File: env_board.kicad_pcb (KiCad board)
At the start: 2 copper layers, 20.7 x 19.2 mm, 22 parts, among them J1 CONN_01X07, J2 BATT_CONN, P1 USB_OTG, Q1 Q_NMOS_GSD, Q2 Q_PMOS_GSD, U1 RFD77101, U2 ENS210, U3 CCS811, U4 AP2204K-3.0, U5 MCP73811T-420I-OT

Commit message: update pcb
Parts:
- removed R1: 10k, Resistors_SMD:R_0603
- P1: footprint Connect:USB_Micro-B -> Connectors_USB:USB_Micro-B_Molex_47346-0001
- moved C2 8.02 mm to (152.3, 109.9), turned to 0 degrees
- moved C6 7.39 mm to (164.7, 115.9), turned to 180 degrees
- moved C5 6.28 mm to (155.7, 108.3), turned to 180 degrees
- moved U3 3.16 mm to (161.1, 114.5), turned to 90 degrees
- moved U2 2.70 mm to (164.7, 113.9), turned to 180 degrees
- moved C7 2.40 mm to (158.2, 114.5), turned to 90 degrees
- moved P1 1.90 mm to (152.8, 114.5)
- moved R2 0.95 mm to (153.0, 107.0)
- moved U5 0.95 mm to (150.1, 107.2)
- moved C3 0.54 mm to (150.4, 104.8)
- moved R7 0.25 mm to (158.7, 109.5)
- moved Q1 0.14 mm to (158.8, 107.0), turned to 180 degrees
- moved U4 0.10 mm to (155.6, 105.8)
- turned Q2 to 270 degrees
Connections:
- C4 pad 1: Net-(C4-Pad1) -> VBUS
- D2 pad 1: Net-(C4-Pad1) -> VBUS
- J1 pad 3: VDD -> VBUS
- Q2 pad 2: Net-(C4-Pad1) -> VBUS
- U1 pad 11: (no net) -> /PowerMgmt/BATT_V_EN
- U1 pad 20: /PowerMgmt/BATT_V_EN -> (no net)
- U1 pad 28: (no net) -> /CCS_WAKE
- U3 pad 2: Net-(R1-Pad2) -> VDD
- U3 pad 7: (no net) -> /CCS_WAKE
- U4 pad 1: Net-(C4-Pad1) -> VBUS
- U4 pad 3: Net-(C4-Pad1) -> VBUS
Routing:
- net /PowerMgmt/BATT_V: track 29.2 -> 5.95 mm
- net VBUS: track 0.00 -> 12.7 mm
- net GND: track 42.8 -> 55.3 mm
- net +BATT: track 6.62 -> 12.2 mm
- net Net-(C2-Pad1): track 15.5 -> 20.5 mm
- net Net-(C4-Pad1): track 4.34 -> 0.00 mm
- net Net-(R1-Pad2): track 3.72 -> 0.00 mm
- net /SDA: track 2.56 -> 0.00 mm
- net Net-(Q1-Pad3): track 0.00 -> 1.78 mm
- net /PowerMgmt/BATT_V_EN: track 0.00 -> 1.68 mm
- net /SCL: track 1.68 -> 0.00 mm
- net VDD: track 22.9 -> 21.6 mm

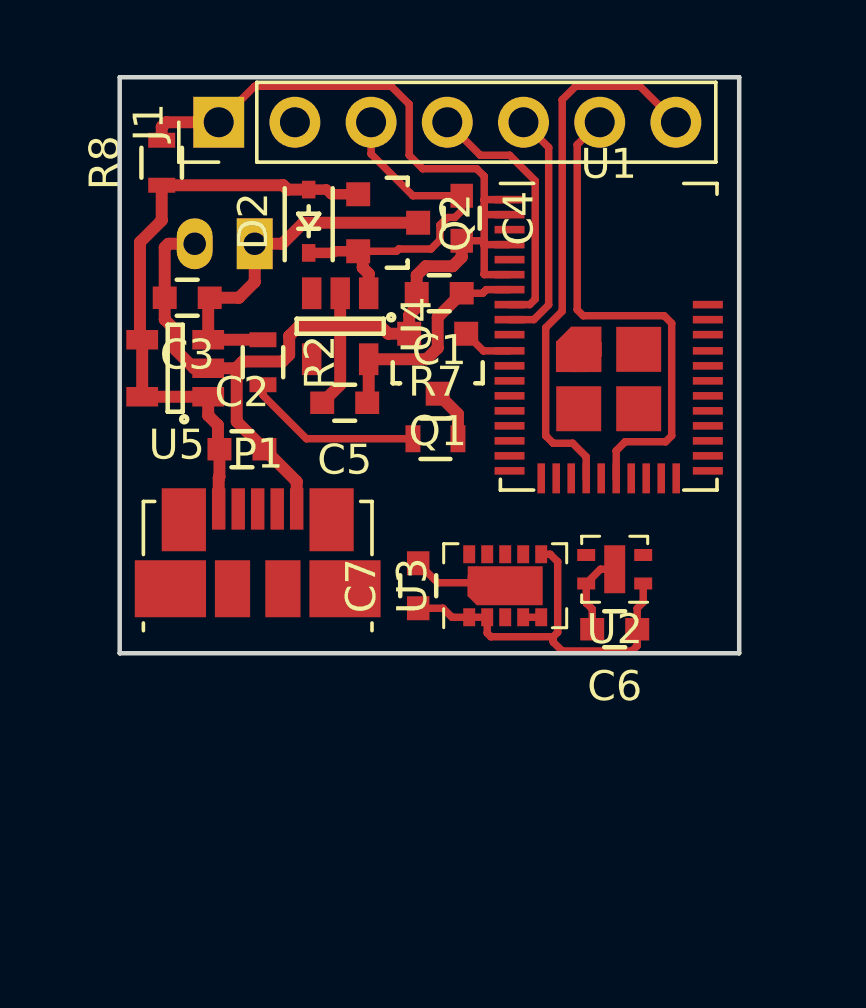
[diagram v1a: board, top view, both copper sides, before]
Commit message: update board, schematics, add bmp280
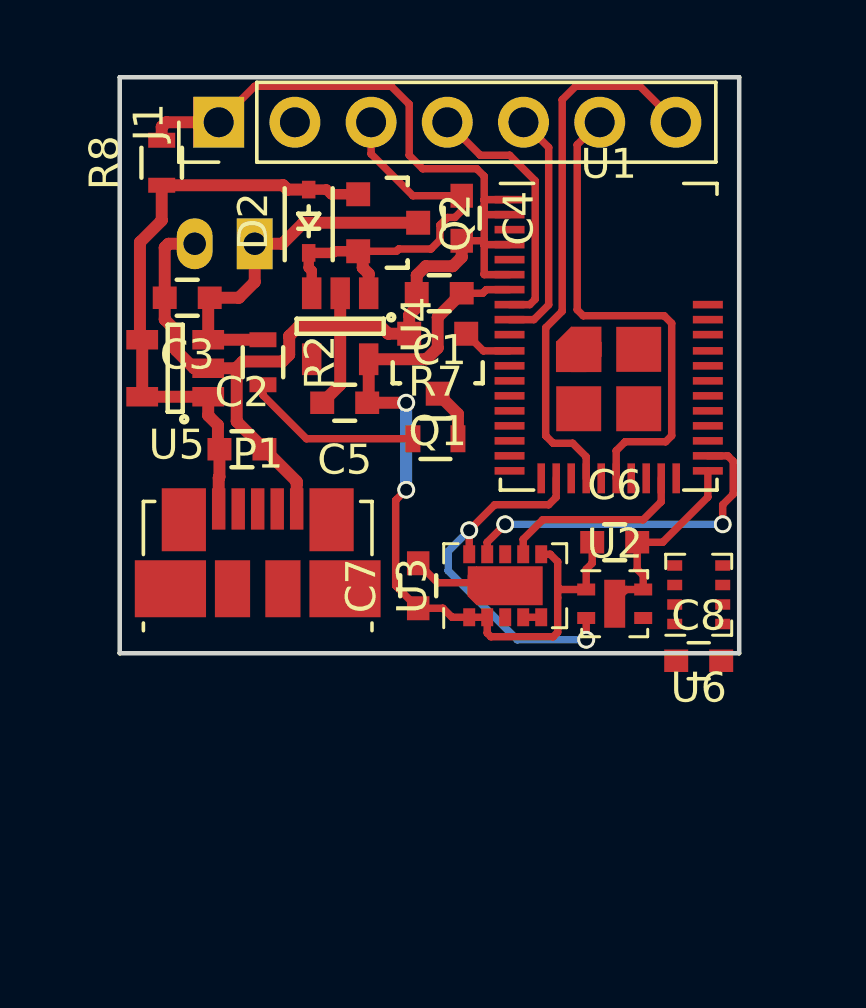
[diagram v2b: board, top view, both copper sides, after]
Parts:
- added C8: 200n, Capacitors_SMD:C_0603, F.Cu at (167.5, 117.0)
- added U6: BMP280, Housings_LGA:Bosch_LGA-8_2x2.5mm_Pitch0.65mm, F.Cu at (167.5, 114.8)
- moved C6 2.90 mm to (164.7, 113.0), turned to 0 degrees
- moved U2 1.15 mm to (164.7, 115.0), turned to 0 degrees
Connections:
- net /PowerMgmt/BATT_V renamed /BATT_V
- net /PowerMgmt/BATT_V_EN renamed /BATT_V_EN
- J1 pad 2: (no net) -> Net-(J1-Pad2)
- P1 pad 2: (no net) -> Net-(P1-Pad2)
- P1 pad 3: (no net) -> Net-(P1-Pad3)
- P1 pad 4: (no net) -> Net-(P1-Pad4)
- U1 pad 10: (no net) -> Net-(U1-Pad10)
- U1 pad 12: (no net) -> Net-(U1-Pad12)
- U1 pad 13: (no net) -> Net-(U1-Pad13)
- U1 pad 14: (no net) -> Net-(U1-Pad14)
- U1 pad 15: (no net) -> Net-(U1-Pad15)
- U1 pad 16: (no net) -> Net-(U1-Pad16)
- U1 pad 17: (no net) -> Net-(U1-Pad17)
- U1 pad 18: (no net) -> Net-(U1-Pad18)
- U1 pad 20: (no net) -> Net-(U1-Pad20)
- U1 pad 24: (no net) -> Net-(U1-Pad24)
- U1 pad 26: (no net) -> Net-(U1-Pad26)
- U1 pad 27: (no net) -> Net-(U1-Pad27)
- U1 pad 29: (no net) -> Net-(U1-Pad29)
- U1 pad 3: (no net) -> Net-(U1-Pad3)
- U1 pad 32: (no net) -> Net-(U1-Pad32)
- U1 pad 33: (no net) -> Net-(U1-Pad33)
- U1 pad 34: (no net) -> Net-(U1-Pad34)
- U1 pad 35: (no net) -> Net-(U1-Pad35)
- U1 pad 36: (no net) -> Net-(U1-Pad36)
- U1 pad 37: (no net) -> Net-(U1-Pad37)
- U1 pad 38: (no net) -> Net-(U1-Pad38)
- U1 pad 39: (no net) -> Net-(U1-Pad39)
- U1 pad 40: (no net) -> Net-(U1-Pad40)
- U1 pad 41: (no net) -> Net-(U1-Pad41)
- U1 pad 5: (no net) -> Net-(U1-Pad5)
- U3 pad 3: (no net) -> /CCS_INT
- U3 pad 8: (no net) -> Net-(U3-Pad8)
- U4 pad 4: (no net) -> Net-(U4-Pad4)
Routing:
- net /SCL: track 0.00 -> 12.7 mm, vias 0 -> 2
- net /SDA: track 0.00 -> 11.7 mm, vias 0 -> 2
- net /CCS_WAKE: track 0.00 -> 6.40 mm
- net VDD: track 21.6 -> 27.6 mm, vias 0 -> 2
- net GND: track 55.3 -> 59.2 mm
- net VBUS: track 12.7 -> 14.1 mm

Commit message: update sensor and add housing for sensor
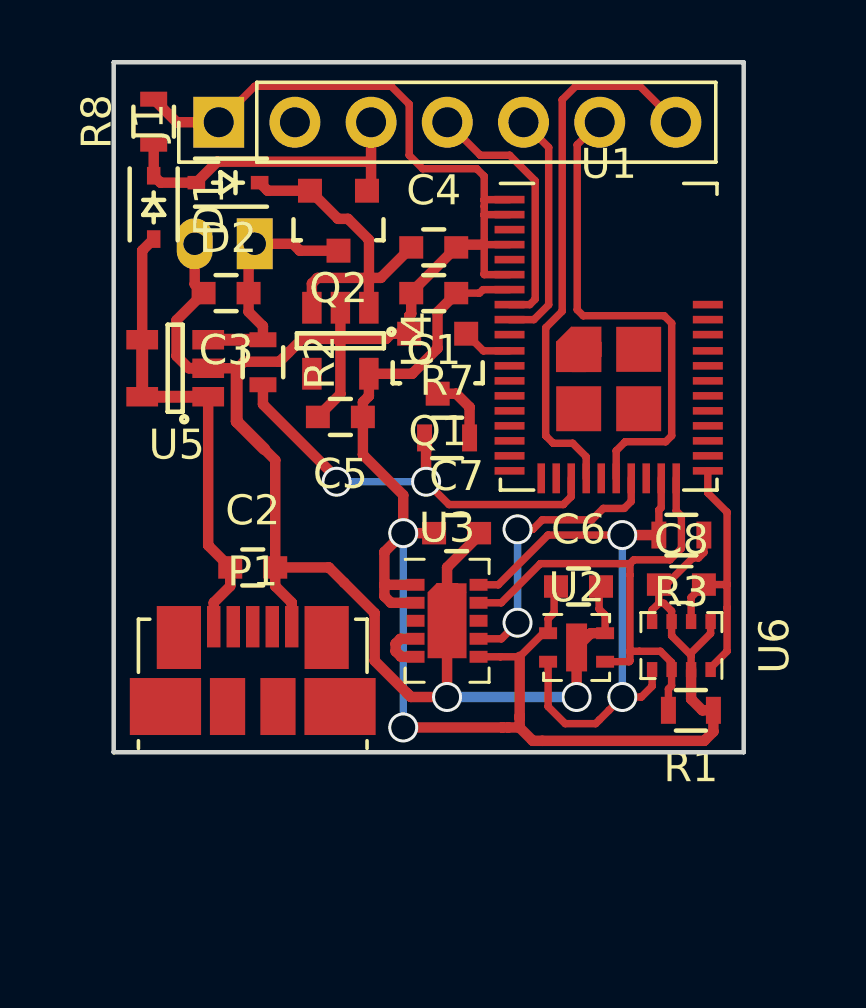
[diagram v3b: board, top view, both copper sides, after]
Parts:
- added D1: BAT20J, Diodes_SMD:SOD-323, F.Cu at (149.3, 101.8)
- added R1: 10k, Resistors_SMD:R_0603, F.Cu at (167.2, 118.6)
- added R3: 10k, Resistors_SMD:R_0603, F.Cu at (166.9, 112.8)
- C5: value 2.2u -> 1u
- U4: value AP2204K-3.0 -> TLV74130
- moved C2 3.96 mm to (152.6, 113.8)
- moved P1 3.93 mm to (152.6, 118.5)
- moved D2 2.98 mm to (151.8, 101.0), turned to 180 degrees
- moved C8 2.60 mm to (166.9, 114.4)
- moved U3 2.26 mm to (159.1, 115.6), turned to 0 degrees
- moved C7 2.17 mm to (159.4, 112.7), turned to 0 degrees
- moved U2 1.93 mm to (163.4, 116.5)
- moved C6 1.91 mm to (163.5, 114.5)
- moved U6 1.79 mm to (166.9, 116.4), turned to 270 degrees
- moved Q2 1.66 mm to (155.5, 102.3), turned to 180 degrees
- moved R8 1.39 mm to (149.3, 99.0)
- moved C4 1.35 mm to (158.7, 103.2), turned to 0 degrees
- moved C3 1.31 mm to (151.7, 104.7)
- moved C5 0.49 mm to (155.6, 108.8)
- moved U4 0.48 mm to (155.6, 106.3)
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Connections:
- net /BATT_V renamed /PowerMgmt/BATT_V
- net /BATT_V_EN renamed /PowerMgmt/BATT_V_EN
- C4 pad 1: VBUS -> Net-(C4-Pad1)
- C8 pad 1: Net-(C8-Pad1) -> VDD
- C8 pad 2: Net-(C8-Pad2) -> GND
- D2 pad 1: VBUS -> Net-(C4-Pad1)
- D2 pad 2: Net-(C2-Pad1) -> VBUS
- J1 pad 2: Net-(J1-Pad2) -> (no net)
- P1 pad 2: Net-(P1-Pad2) -> (no net)
- P1 pad 3: Net-(P1-Pad3) -> (no net)
- P1 pad 4: Net-(P1-Pad4) -> (no net)
- Q2 pad 1: Net-(C2-Pad1) -> VBUS
- Q2 pad 2: VBUS -> Net-(C4-Pad1)
- R8 pad 1: Net-(C2-Pad1) -> VBUS
- U1 pad 10: Net-(U1-Pad10) -> (no net)
- U1 pad 12: Net-(U1-Pad12) -> (no net)
- U1 pad 13: Net-(U1-Pad13) -> (no net)
- U1 pad 14: Net-(U1-Pad14) -> (no net)
- U1 pad 15: Net-(U1-Pad15) -> (no net)
- U1 pad 16: Net-(U1-Pad16) -> (no net)
- U1 pad 17: Net-(U1-Pad17) -> (no net)
- U1 pad 18: Net-(U1-Pad18) -> (no net)
- U1 pad 20: Net-(U1-Pad20) -> (no net)
- U1 pad 21: /SCL -> (no net)
- U1 pad 24: Net-(U1-Pad24) -> (no net)
- U1 pad 26: Net-(U1-Pad26) -> /CCS_WAKE
- U1 pad 27: Net-(U1-Pad27) -> (no net)
- U1 pad 28: /CCS_WAKE -> /SCL
- U1 pad 29: Net-(U1-Pad29) -> /SDA
- U1 pad 3: Net-(U1-Pad3) -> (no net)
- U1 pad 31: /SDA -> (no net)
- U1 pad 32: Net-(U1-Pad32) -> (no net)
- U1 pad 33: Net-(U1-Pad33) -> (no net)
- U1 pad 34: Net-(U1-Pad34) -> (no net)
- U1 pad 35: Net-(U1-Pad35) -> (no net)
- U1 pad 36: Net-(U1-Pad36) -> (no net)
- U1 pad 37: Net-(U1-Pad37) -> (no net)
- U1 pad 38: Net-(U1-Pad38) -> (no net)
- U1 pad 39: Net-(U1-Pad39) -> (no net)
- U1 pad 40: Net-(U1-Pad40) -> (no net)
- U1 pad 41: Net-(U1-Pad41) -> (no net)
- U1 pad 5: Net-(U1-Pad5) -> (no net)
- U3 pad 3: /CCS_INT -> (no net)
- U3 pad 8: Net-(U3-Pad8) -> (no net)
- U4 pad 1: VBUS -> Net-(C4-Pad1)
- U4 pad 3: VBUS -> Net-(C4-Pad1)
- U4 pad 4: Net-(U4-Pad4) -> (no net)
- U6 pad 1: Net-(C8-Pad2) -> GND
- U6 pad 2: Net-(C8-Pad1) -> VDD
- U6 pad 5: Net-(C8-Pad1) -> VDD
- U6 pad 6: Net-(C8-Pad1) -> VDD
- U6 pad 7: Net-(C8-Pad2) -> GND
- U6 pad 8: Net-(C8-Pad1) -> VDD
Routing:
- net GND: track 59.2 -> 84.6 mm, vias 0 -> 2
- net VDD: track 27.6 -> 52.5 mm
- net Net-(C4-Pad1): track 0.00 -> 11.3 mm
- net /PowerMgmt/BATT_V: track 5.95 -> 14.6 mm, vias 0 -> 2
- net /SCL: track 12.7 -> 20.3 mm
- net /SDA: track 11.7 -> 17.2 mm, vias 2 -> 0
- net Net-(C2-Pad1): track 20.5 -> 15.9 mm
- net +BATT: track 12.2 -> 8.40 mm
- net /CCS_WAKE: track 6.40 -> 9.58 mm, vias 0 -> 2
- net VBUS: track 14.1 -> 11.0 mm
- net Net-(U3-Pad4): track 0.60 -> 1.73 mm
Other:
- board size 20.7 x 19.2 mm -> 21 x 23 mm

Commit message: update sensor/housings
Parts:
- added Q3: DMP3099L-13, Package_TO_SOT_SMD:SOT-23, F.Cu at (155.0, 114.6)
- added R4: 10k, Resistor_SMD:R_0603_1608Metric, F.Cu at (154.8, 119.2)
- added R5: 10k, Resistor_SMD:R_0603_1608Metric, F.Cu at (154.9, 112.1)
- C1, C2, C3, C4, C5, C6, C7, C8: footprint Capacitors_SMD:C_0603 -> Capacitor_SMD:C_0603_1608Metric
- D1, D2: footprint Diodes_SMD:SOD-323 -> Diode_SMD:D_SOD-323
- J1: footprint Pin_Headers:Pin_Header_Straight_1x07_Pitch2.54mm -> Connector_PinHeader_2.54mm:PinHeader_1x07_P2.54mm_Vertical
- J2: footprint Connectors_JST:JST_PH_S2B-PH-K_02x2.00mm_Angled -> Connector_JST:JST_PH_S2B-PH-K_1x02_P2.00mm_Horizontal
- P1: footprint Connectors_USB:USB_Micro-B_Molex_47346-0001 -> Connector_USB:USB_Micro-B_Molex_47346-0001
- Q1: value Q_NMOS_GSD -> NX7002AKVL; footprint TO_SOT_Packages_SMD:SOT-23 -> Package_TO_SOT_SMD:SOT-23
- Q2: value Q_PMOS_GSD -> DMP3099L-13; footprint TO_SOT_Packages_SMD:SOT-23 -> Package_TO_SOT_SMD:SOT-23
- R1, R2, R3, R7, R8: footprint Resistors_SMD:R_0603 -> Resistor_SMD:R_0603_1608Metric
- U1: footprint kicad-RF_Modules:RFDigital_RFD77101 -> RF_Module:RFDigital_RFD77101
- U2: footprint Housings_DFN_QFN:AMS_QFN-4-1EP_2x2mm_Pitch0.95mm -> Package_DFN_QFN:AMS_QFN-4-1EP_2x2mm_P0.95mm_EP0.7x1.6mm
- U3: footprint kicad-Housings_LGA:AMS_LGA-10-1EP_2.7x4mm_Pitch0.6mm -> Package_LGA:AMS_LGA-10-1EP_2.7x4mm_P0.6mm
- U4, U5: footprint TO_SOT_Packages_SMD:SOT-23-5 -> Package_TO_SOT_SMD:SOT-23-5
- U6: footprint Housings_LGA:Bosch_LGA-8_2x2.5mm_Pitch0.65mm -> Package_LGA:Bosch_LGA-8_2x2.5mm_P0.65mm_ClockwisePinNumbering
- moved R3 12.9 mm to (160.3, 123.8), turned to 0 degrees
- moved R2 10.0 mm to (158.3, 115.5), turned to 0 degrees
- moved R1 5.43 mm to (165.7, 123.8)
- moved C7 5.37 mm to (157.5, 117.7)
- moved U3 5.30 mm to (157.5, 120.7)
- moved P1 5.21 mm to (148.9, 114.9), turned to 270 degrees
- moved U6 4.91 mm to (165.7, 121.2)
- moved C6 4.82 mm to (162.4, 119.2)
- moved U2 4.82 mm to (162.4, 121.2)
- moved C8 4.61 mm to (165.7, 118.9), turned to 180 degrees
- moved R7 4.51 mm to (158.3, 114.0), turned to 180 degrees
- moved C4 4.26 mm to (154.9, 105.2)
- moved Q1 3.62 mm to (158.6, 110.7), turned to 270 degrees
- moved D2 2.95 mm to (154.4, 102.4), turned to 90 degrees
- moved C5 1.83 mm to (154.9, 110.5)
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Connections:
- net /PowerMgmt/BATT_V renamed /BATT_V
- net /PowerMgmt/BATT_V_EN renamed /BATT_V_EN
- R2 pad 1: +BATT -> Net-(Q3-Pad3)
- R7 pad 2: Net-(Q1-Pad3) -> GND
- U1 pad 24: (no net) -> /SDA
- U1 pad 29: /SDA -> (no net)
- U3 pad 2: VDD -> Net-(R4-Pad2)
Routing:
- net /SCL: track 20.3 -> 39.6 mm
- net /SDA: track 17.2 -> 29.1 mm, vias 0 -> 2
- net +BATT: track 8.40 -> 19.1 mm
- net VDD: track 52.5 -> 60.6 mm, vias 2 -> 0
- net GND: track 84.6 -> 92.4 mm, vias 2 -> 3
- net /BATT_V: track 14.6 -> 7.37 mm, vias 2 -> 0
- net /CCS_WAKE: track 9.58 -> 14.9 mm, vias 2 -> 0
- net /BATT_V_EN: track 1.68 -> 4.16 mm
- net Net-(Q3-Pad3): track 0.00 -> 2.47 mm
- net Net-(C4-Pad1): track 11.3 -> 9.00 mm
- net Net-(Q1-Pad3): track 2.27 -> 4.58 mm
- net Net-(R4-Pad2): track 0.00 -> 1.69 mm
- net Net-(C2-Pad1): track 15.9 -> 14.7 mm
- added copper zone on F.Cu, net GND
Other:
- board size 21 x 23 mm -> 23.3 x 29.2 mm

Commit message: update pcb
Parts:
- added G***: LOGO, SoilMeasuringBoard:TU_Logo_Framed, B.Cu at (162.4, 105.7)
- moved R3 0.87 mm to (160.5, 124.7)
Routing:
- net GND: track 92.4 -> 94.8 mm, vias 3 -> 10
- net VDD: track 60.6 -> 62.7 mm
- added copper zone on B.Cu, net GND
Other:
- board size 23.3 x 29.2 mm -> 22.5 x 29 mm
